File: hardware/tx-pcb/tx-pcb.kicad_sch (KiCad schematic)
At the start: 37 parts, among them J1 SWD_Pins, J2 RF_Module_Conn, J3 USB2.0_C_16P, J4 Conn_Coaxial_Small, SW1 BOOT0, SW2 RESET, U1 STM32WB55CEUx, U2 USBLC6-2SC6, X1 CS11336-32M, X2 ABS07-32.768KHZ-1-T

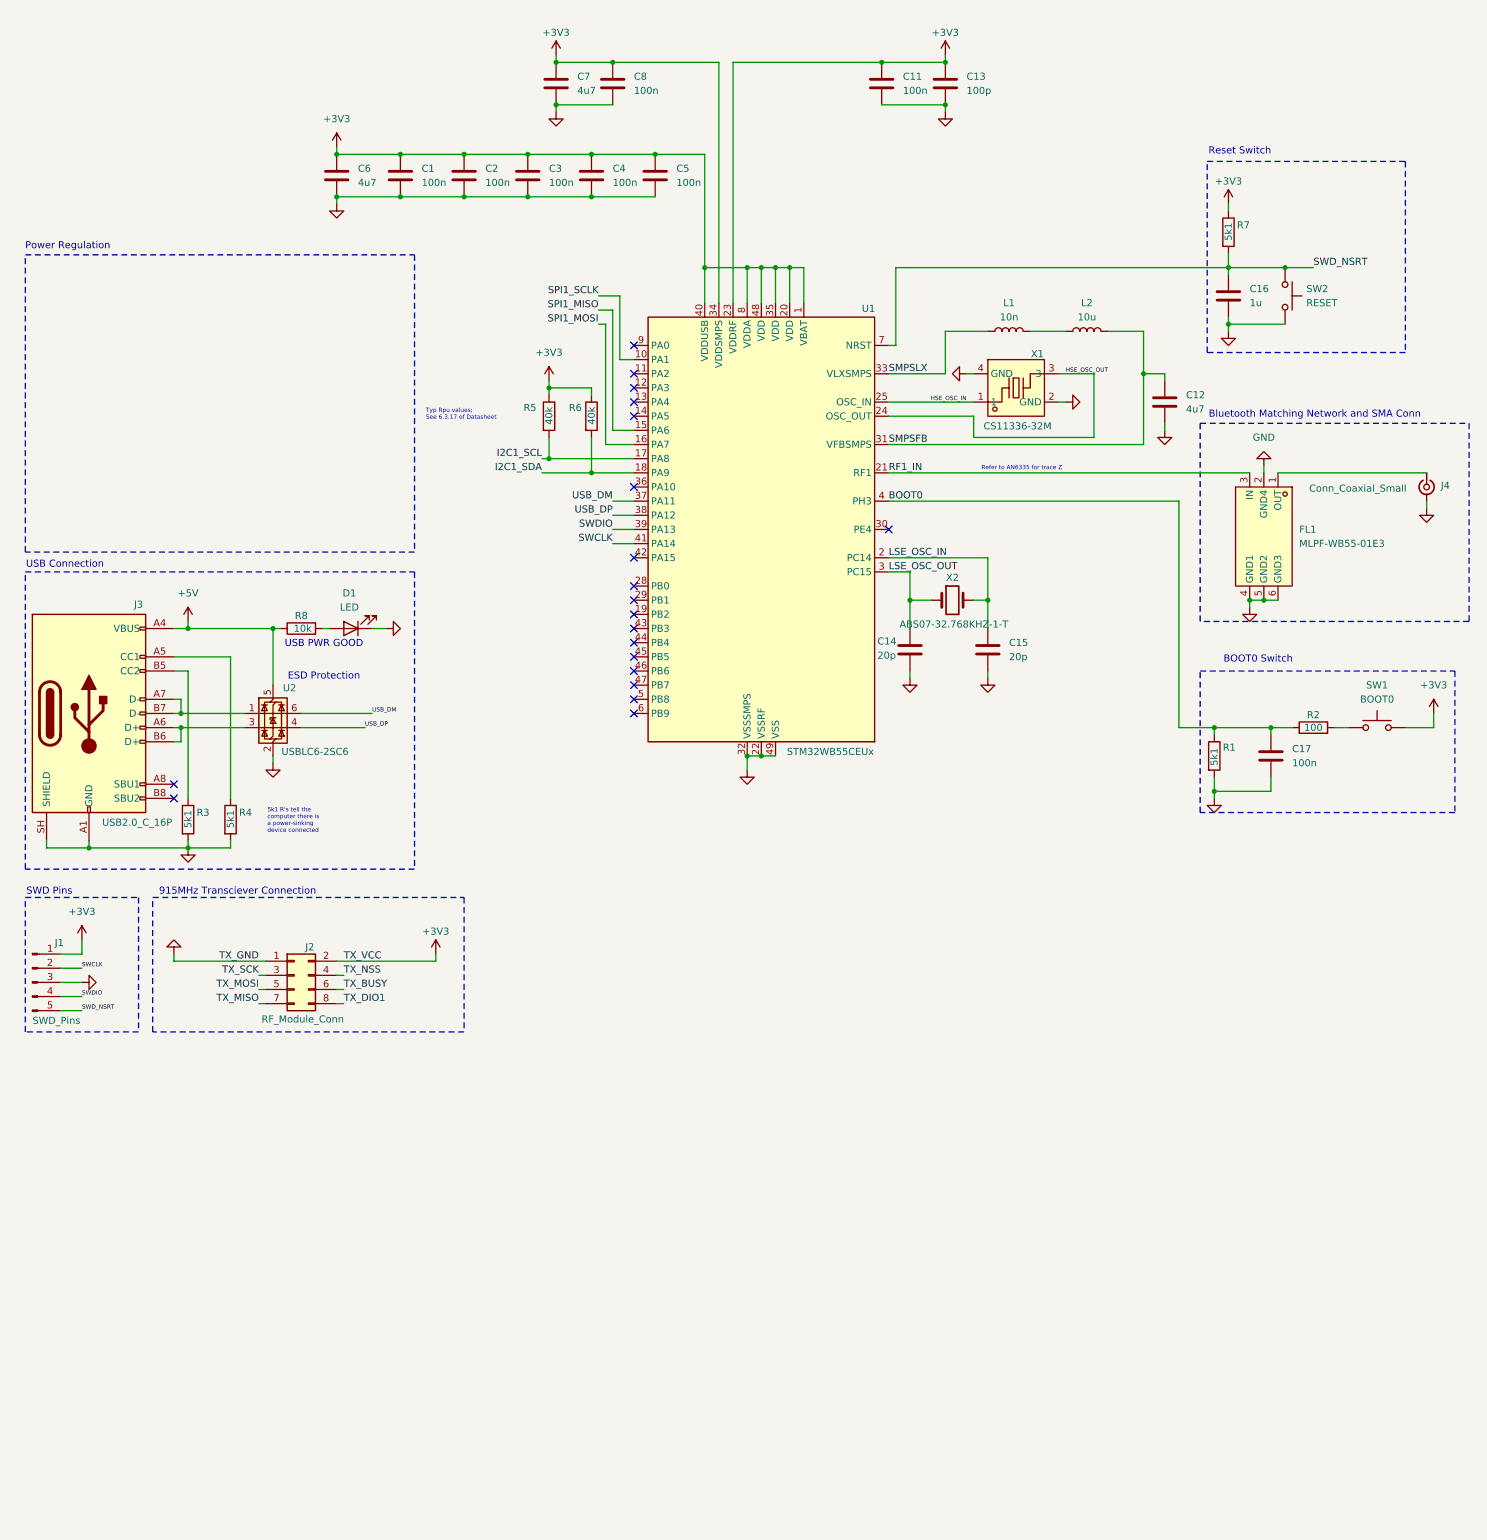
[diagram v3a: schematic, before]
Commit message: added footprints, completed schematics but still need V reg
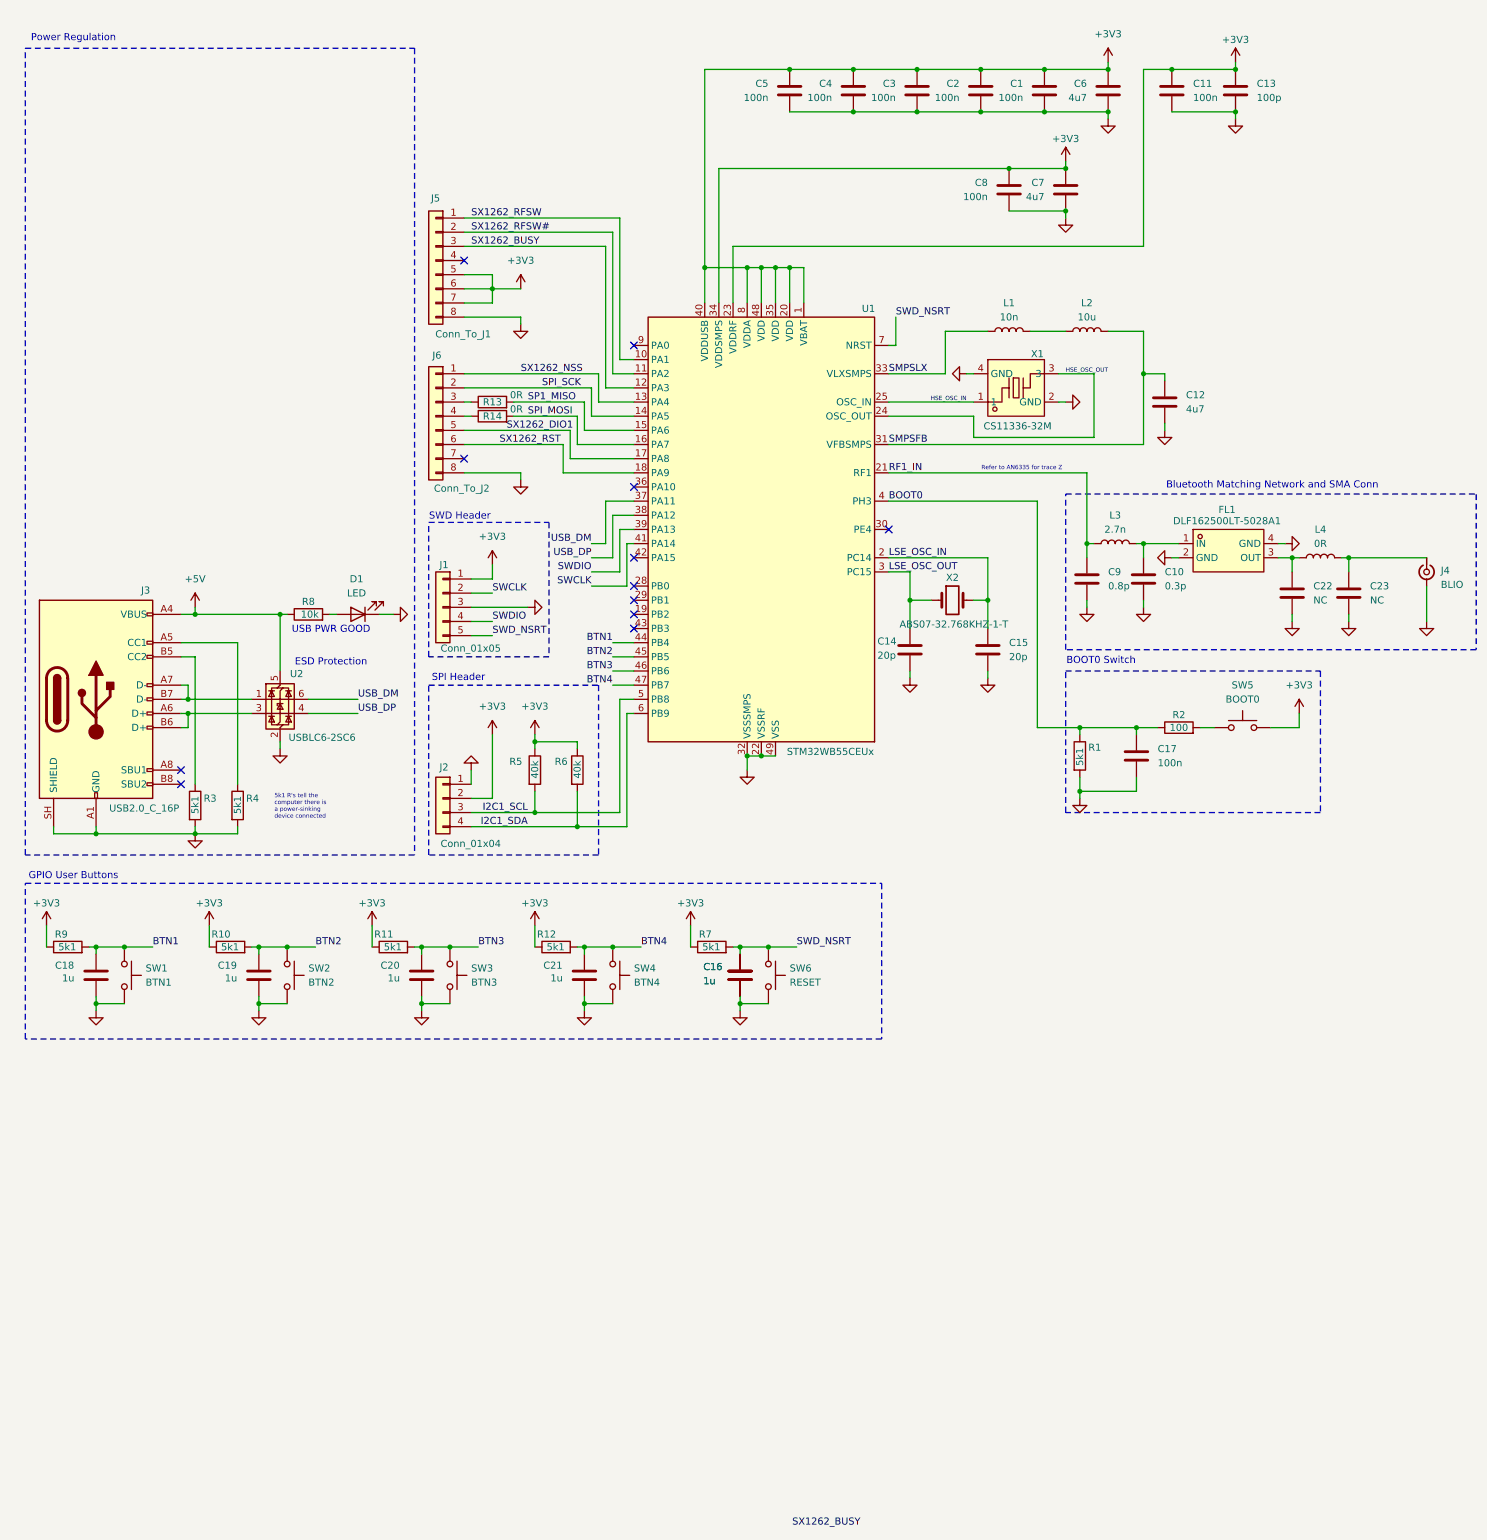
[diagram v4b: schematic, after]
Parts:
- removed FL1: MLPF-WB55-01E3, rf-pwr-tx-library:FILTER-SMD_6P-L1.6-W1.0-P0.50-BL, symbol easyeda2kicad:MLPF-WB55-01E3
- removed J1: SWD_Pins, Connector_PinSocket_2.54mm:PinSocket_1x05_P2.54mm_Vertical, symbol Connector:Conn_01x05_Pin
- removed J2: RF_Module_Conn, Connector_PinHeader_2.00mm:PinHeader_2x04_P2.00mm_Vertical, symbol Connector_Generic:Conn_02x04_Odd_Even
- added C10: 0.3p, symbol Device:C
- added C18, C19, C20, C21: 1u, Capacitor_SMD:C_0603_1608Metric_Pad1.08x0.95mm_HandSolder, symbol Device:C
- added C22, C23: NC, symbol Device:C
- added C9: 0.8p, symbol Device:C
- added FL1: DLF162500LT-5028A1, easyeda2kicad:FILTER-SMD_0603-4P-L1.6-W0.8-L-1, symbol easyeda2kicad:DLF162500LT-5028A1
- added J1: Conn_01x05, symbol Connector_Generic:Conn_01x05
- added J2: Conn_01x04, Connector_PinHeader_1.27mm:PinHeader_1x04_P1.27mm_Vertical, symbol Connector_Generic:Conn_01x04
- added J5: Conn_To_J1, Connector_PinHeader_1.27mm:PinHeader_1x08_P1.27mm_Vertical, symbol Connector_Generic:Conn_01x08
- added J6: Conn_To_J2, Connector_PinHeader_1.27mm:PinHeader_1x08_P1.27mm_Vertical, symbol Connector_Generic:Conn_01x08
- added L3: 2.7n, symbol Device:L
- added L4: 0R, symbol Device:L
- added R10, R11, R12, R9: 5k1, Resistor_SMD:R_0805_2012Metric_Pad1.20x1.40mm_HandSolder, symbol Device:R
- added R13, R14: 0R, symbol Device:R
- added SW1: BTN1, Button_Switch_THT:SW_PUSH_6mm, symbol Switch:SW_Push
- added SW2: BTN2, Button_Switch_THT:SW_PUSH_6mm, symbol Switch:SW_Push
- added SW3: BTN3, Button_Switch_THT:SW_PUSH_6mm, symbol Switch:SW_Push
- added SW4: BTN4, Button_Switch_THT:SW_PUSH_6mm, symbol Switch:SW_Push
- J4: value Conn_Coaxial_Small -> BLIO
- renumbered SW1 to SW5, SW2 to SW6
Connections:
- net +3V3: now also J1.1 (Pin_1), J2.2 (Pin_2), J5.5 (Pin_5), J5.6 (Pin_6), J5.7 (Pin_7), R10.1, R11.1, R12.1, R9.1
- net GND: now also C10.2, C18.2, C19.2, C20.2, C21.2, C22.2, C23.2, C9.2, FL1.2 (GND), FL1.4 (GND), J1.3 (Pin_3), J2.1 (Pin_1), J5.8 (Pin_8), J6.8 (Pin_8), SW1.2, SW2.2, SW3.2, SW4.2
- net I2C1_SCL: now also U1.5 (PB8), J2.3 (Pin_3); no longer U1.17 (PA8)
- net I2C1_SDA: now also U1.6 (PB9), J2.4 (Pin_4); no longer U1.18 (PA9)
- net RF1_IN: now also C9.1, L3.1
- net SWCLK: now also J1.2 (Pin_2)
- net SWDIO: now also J1.4 (Pin_4)
- net SWD_NSRT: now also J1.5 (Pin_5)
- net at J4.1 (In): now also C23.1, L4.2
- net SX1262_RFSW#: now reaches U1.11 (PA2)
- net SX1262_RFSW#: now also J5.2 (Pin_2)
- net SX1262_BUSY: now reaches U1.12 (PA3)
- net SX1262_BUSY: now also J5.3 (Pin_3)
- net SX1262_NSS: now reaches U1.13 (PA4)
- net SX1262_NSS: now also J6.1 (Pin_1)
- net SPI_SCK: now reaches U1.14 (PA5)
- net SPI_SCK: now also J6.2 (Pin_2)
- net BTN1: now reaches U1.44 (PB4)
- net BTN1: now also C18.1, R9.2, SW1.1
- net BTN2: now reaches U1.45 (PB5)
- net BTN2: now also C19.1, R10.2, SW2.1
- net BTN3: now reaches U1.46 (PB6)
- net BTN3: now also C20.1, R11.2, SW3.1
- net BTN4: now reaches U1.47 (PB7)
- net BTN4: now also C21.1, R12.2, SW4.1
- net SPI1_MISO renamed SP1_MISO
- net SP1_MISO: now also R13.2
- net SPI1_MOSI renamed SPI_MOSI
- net SPI_MOSI: now also R14.2
- net SPI1_SCLK renamed SX1262_RFSW
- net SX1262_RFSW: now also J5.1 (Pin_1)
- new net: C22.1, FL1.3 (OUT), L4.1
- new net: C10.1, FL1.1 (IN), L3.2
- new net: J6.4 (Pin_4), R14.1
- new net: J6.3 (Pin_3), R13.1
- new net SX1262_DIO1: J6.5 (Pin_5), U1.17 (PA8)
- new net SX1262_RST: J6.6 (Pin_6), U1.18 (PA9)
- no-connect marks 20 -> 12
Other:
- note added: "GPIO User Buttons"
- note added: "SPI Header"
- note added: "SWD Header"
- note removed: "915MHz Transciever Connection"
- note removed: "Reset Switch"
- note removed: "SWD Pins"
- note removed: "Typ Rpu values; See 6.3.17 of Datasheet"
- note removed: "USB Connection"
- moved on the sheet: C1, C11, C13, C16, C17, C2, C3, C4, C5, C6, C7, C8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

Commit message: began layout
began layout, updated schematic USB and input switches
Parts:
- removed J3: USB2.0_C_16P, rf-pwr-tx-library:USB-C-SMD_GT-USB-7047A, symbol Connector:USB_C_Receptacle_USB2.0_16P
- removed R3, R4: 5k1, Resistor_SMD:R_0805_2012Metric_Pad1.20x1.40mm_HandSolder, symbol Device:R
- removed R8: 10k, Resistor_SMD:R_0805_2012Metric_Pad1.20x1.40mm_HandSolder, symbol Device:R
- removed U2: USBLC6-2SC6, Package_TO_SOT_SMD:SOT-23-6, symbol Power_Protection:USBLC6-2SC6
- added C24: 1u, Capacitor_SMD:C_0603_1608Metric_Pad1.08x0.95mm_HandSolder, symbol Device:C
- added R1: 10k, Resistor_SMD:R_0805_2012Metric_Pad1.20x1.40mm_HandSolder, symbol Device:R
- added R14, R2: 5k1, Resistor_SMD:R_0805_2012Metric_Pad1.20x1.40mm_HandSolder, symbol Device:R
- added SW7: BTN5, Button_Switch_THT:SW_PUSH_6mm, symbol Switch:SW_Push
- added U1: USBLC6-2SC6, Package_TO_SOT_SMD:SOT-23-6, symbol Power_Protection:USBLC6-2SC6
- added USB1: GT-USB-7047A, easyeda2kicad:USB-C-SMD_GT-USB-7047A, symbol rf-pwr-tx-library:GT-USB-7047A
- C12: renamed from C9; footprint (none) -> Capacitor_SMD:C_0603_1608Metric_Pad1.08x0.95mm_HandSolder
- C13: renamed from C10; footprint (none) -> Capacitor_SMD:C_0603_1608Metric_Pad1.08x0.95mm_HandSolder
- C14: renamed from C22; footprint (none) -> Capacitor_SMD:C_0603_1608Metric_Pad1.08x0.95mm_HandSolder
- C15: renamed from C23; footprint (none) -> Capacitor_SMD:C_0603_1608Metric_Pad1.08x0.95mm_HandSolder
- FL1: footprint easyeda2kicad:FILTER-SMD_0603-4P-L1.6-W0.8-L-1 -> rf-pwr-tx-library:FILTER-SMD_6P-L1.6-W1.0-P0.50-BL
- J1: renamed from J5; footprint Connector_PinHeader_1.27mm:PinHeader_1x08_P1.27mm_Vertical -> Connector_PinHeader_2.54mm:PinHeader_1x08_P2.54mm_Vertical
- J2: renamed from J6; footprint Connector_PinHeader_1.27mm:PinHeader_1x08_P1.27mm_Vertical -> Connector_PinHeader_2.54mm:PinHeader_1x08_P2.54mm_Vertical
- J4: renamed from J1; footprint (none) -> Connector_PinHeader_2.54mm:PinHeader_1x05_P2.54mm_Vertical
- J5: renamed from J2; footprint Connector_PinHeader_1.27mm:PinHeader_1x04_P1.27mm_Vertical -> Connector_PinHeader_2.54mm:PinHeader_1x04_P2.54mm_Vertical
- L3, L4: footprint (none) -> Inductor_SMD:L_0805_2012Metric_Pad1.05x1.20mm_HandSolder
- R3: renamed from R13; footprint (none) -> Resistor_SMD:R_0805_2012Metric_Pad1.20x1.40mm_HandSolder
- R4: renamed from R14; footprint (none) -> Resistor_SMD:R_0805_2012Metric_Pad1.20x1.40mm_HandSolder
- renumbered C5 to C1, C7 to C10, C12 to C11, C14 to C16, C15 to C17, C17 to C18, C16 to C19, C4 to C2, C18 to C20, C19 to C21, C20 to C22, C21 to C23, C2 to C4, C1 to C5, C11 to C7, C13 to C8, C8 to C9, J4 to J3, R9 to R10, R10 to R11, R11 to R12, R12 to R13, R2 to R5, R7 to R6, R1 to R7, R5 to R8, R6 to R9, SW5 to SW1, SW6 to SW2, SW1 to SW3, SW2 to SW4, SW3 to SW5, SW4 to SW6, U1 to U2
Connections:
- net +3V3: now also R14.1
- net BTN1: now also U2.43 (PB3); no longer U2.44 (PB4)
- net BTN2: now also U2.44 (PB4); no longer U2.45 (PB5)
- net BTN3: now also U2.45 (PB5); no longer U2.46 (PB6)
- net BTN4: now also U2.46 (PB6); no longer U2.47 (PB7)
- net GND: now also C24.2, R2.2, SW7.2, U1.2 (GND), USB1.1 (SHELL), USB1.2 (SHELL), USB1.3 (SHELL), USB1.4 (SHELL), USB1.A1B12 (GND), USB1.B1A12 (GND)
- net USB_DM: now also U1.6 (I/O1)
- net USB_DP: now also U1.4 (I/O2)
- net at D1.2 (A): now also R1.2
- new net: R1.1, U1.5 (VBUS), USB1.A4B9 (VBUS), USB1.B4A9 (VBUS)
- new net: R2.1, USB1.A5 (CC1), USB1.B5 (CC2)
- new net: U1.3 (I/O2), USB1.A6 (DP1), USB1.B6 (DP2)
- new net: U1.1 (I/O1), USB1.A7 (DN1), USB1.B7 (DN2)
- new net BTN5: C24.1, R14.2, SW7.1, U2.47 (PB7)
- no-connect marks 12 -> 11
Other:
- note added: "Reset Switch"
- moved on the sheet: C19, R6, SW2

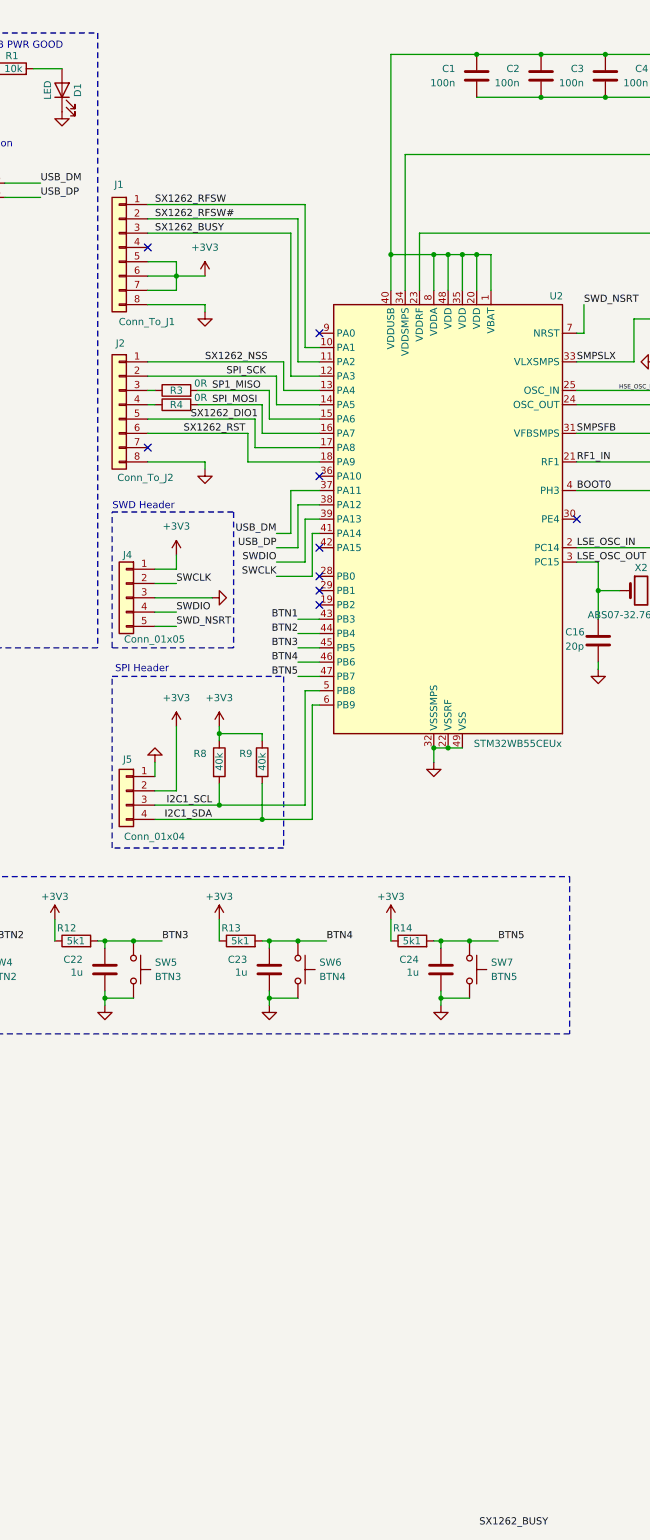
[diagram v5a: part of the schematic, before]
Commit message: worked on transmitter layout
updated transmitter schematic to use the sx1262 dev board over the chip
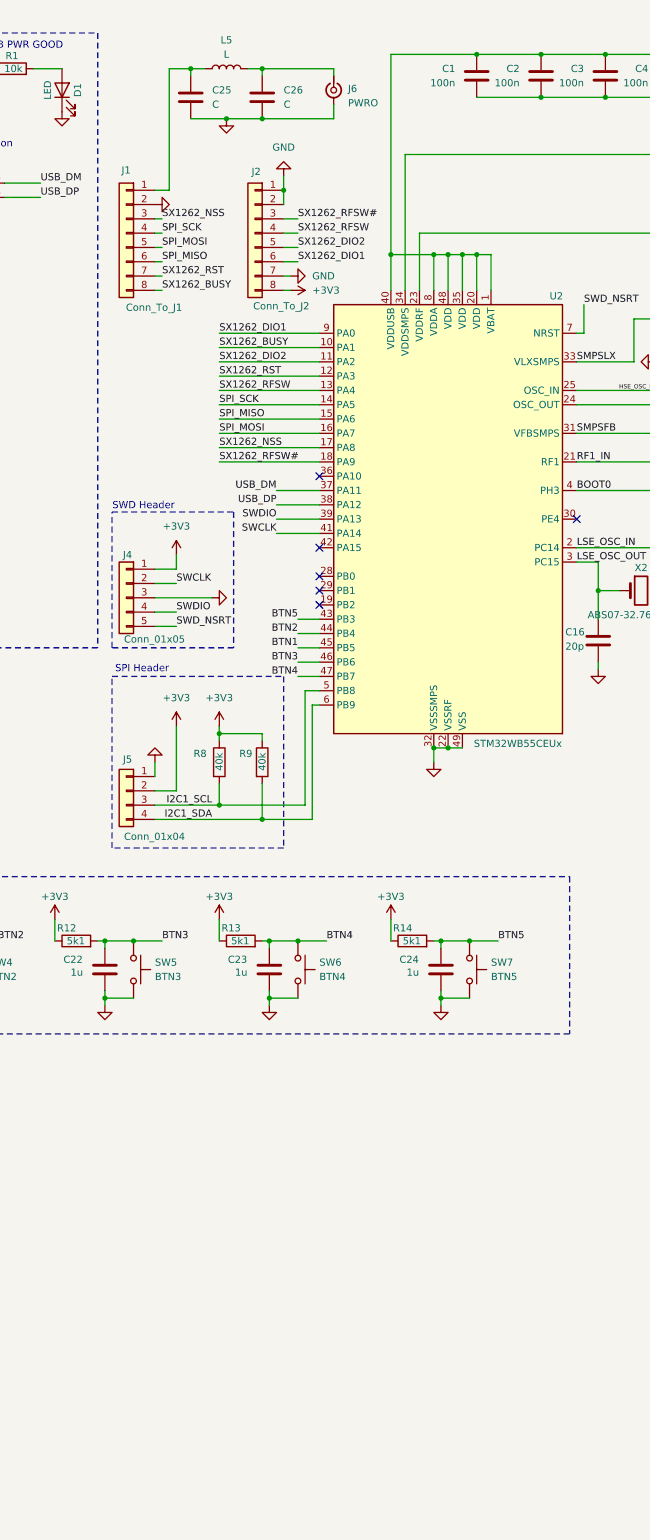
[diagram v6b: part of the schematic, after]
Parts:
- removed R3, R4: 0R, Resistor_SMD:R_0805_2012Metric_Pad1.20x1.40mm_HandSolder, symbol Device:R
- added C25, C26: C, Capacitor_SMD:C_0603_1608Metric_Pad1.08x0.95mm_HandSolder, symbol Device:C
- added J6: PWRO, Connector_Coaxial:SMA_BAT_Wireless_BWSMA-KWE-Z001, symbol Connector:Conn_Coaxial_Small
- added L5: L, Inductor_SMD:L_0805_2012Metric_Pad1.05x1.20mm_HandSolder, symbol Device:L
- USB1: footprint easyeda2kicad:USB-C-SMD_GT-USB-7047A -> rf-pwr-tx-library:USB-C-SMD_GT-USB-7047A
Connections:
- net +3V3: now also J2.8 (Pin_8); no longer J1.5 (Pin_5), J1.6 (Pin_6), J1.7 (Pin_7)
- net BTN1: now also U2.45 (PB5); no longer U2.43 (PB3)
- net BTN3: now also U2.46 (PB6); no longer U2.45 (PB5)
- net BTN4: now also U2.47 (PB7); no longer U2.46 (PB6)
- net BTN5: now also U2.43 (PB3); no longer U2.47 (PB7)
- net GND: now also J1.2 (Pin_2), J2.1 (Pin_1), J2.2 (Pin_2), J2.7 (Pin_7), C25.2, C26.2, J6.2 (Ext); no longer J1.8 (Pin_8), J2.8 (Pin_8)
- net SPI_MOSI: now also J1.5 (Pin_5)
- net SPI_SCK: now also J1.4 (Pin_4); no longer J2.2 (Pin_2)
- net SX1262_BUSY: now also J1.8 (Pin_8), U2.10 (PA1); no longer J1.3 (Pin_3), U2.12 (PA3)
- net SX1262_DIO1: now also J2.6 (Pin_6), U2.9 (PA0); no longer J2.5 (Pin_5), U2.17 (PA8)
- net SX1262_NSS: now also J1.3 (Pin_3), U2.17 (PA8); no longer J2.1 (Pin_1), U2.13 (PA4)
- net SX1262_RFSW: now also J2.4 (Pin_4), U2.13 (PA4); no longer J1.1 (Pin_1), U2.10 (PA1)
- net SX1262_RFSW#: now also J2.3 (Pin_3), U2.18 (PA9); no longer J1.2 (Pin_2), U2.11 (PA2)
- net SX1262_RST: now also J1.7 (Pin_7), U2.12 (PA3); no longer J2.6 (Pin_6), U2.18 (PA9)
- net SP1_MISO renamed SPI_MISO
- net SPI_MISO: now also J1.6 (Pin_6)
- new net: C25.1, J1.1 (Pin_1), L5.1
- new net: C26.1, J6.1 (In), L5.2
- new net SX1262_DIO2: J2.5 (Pin_5), U2.11 (PA2)
- no-connect marks 11 -> 8
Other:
- moved on the sheet: J1, J2
